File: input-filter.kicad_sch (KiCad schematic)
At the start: 28 parts

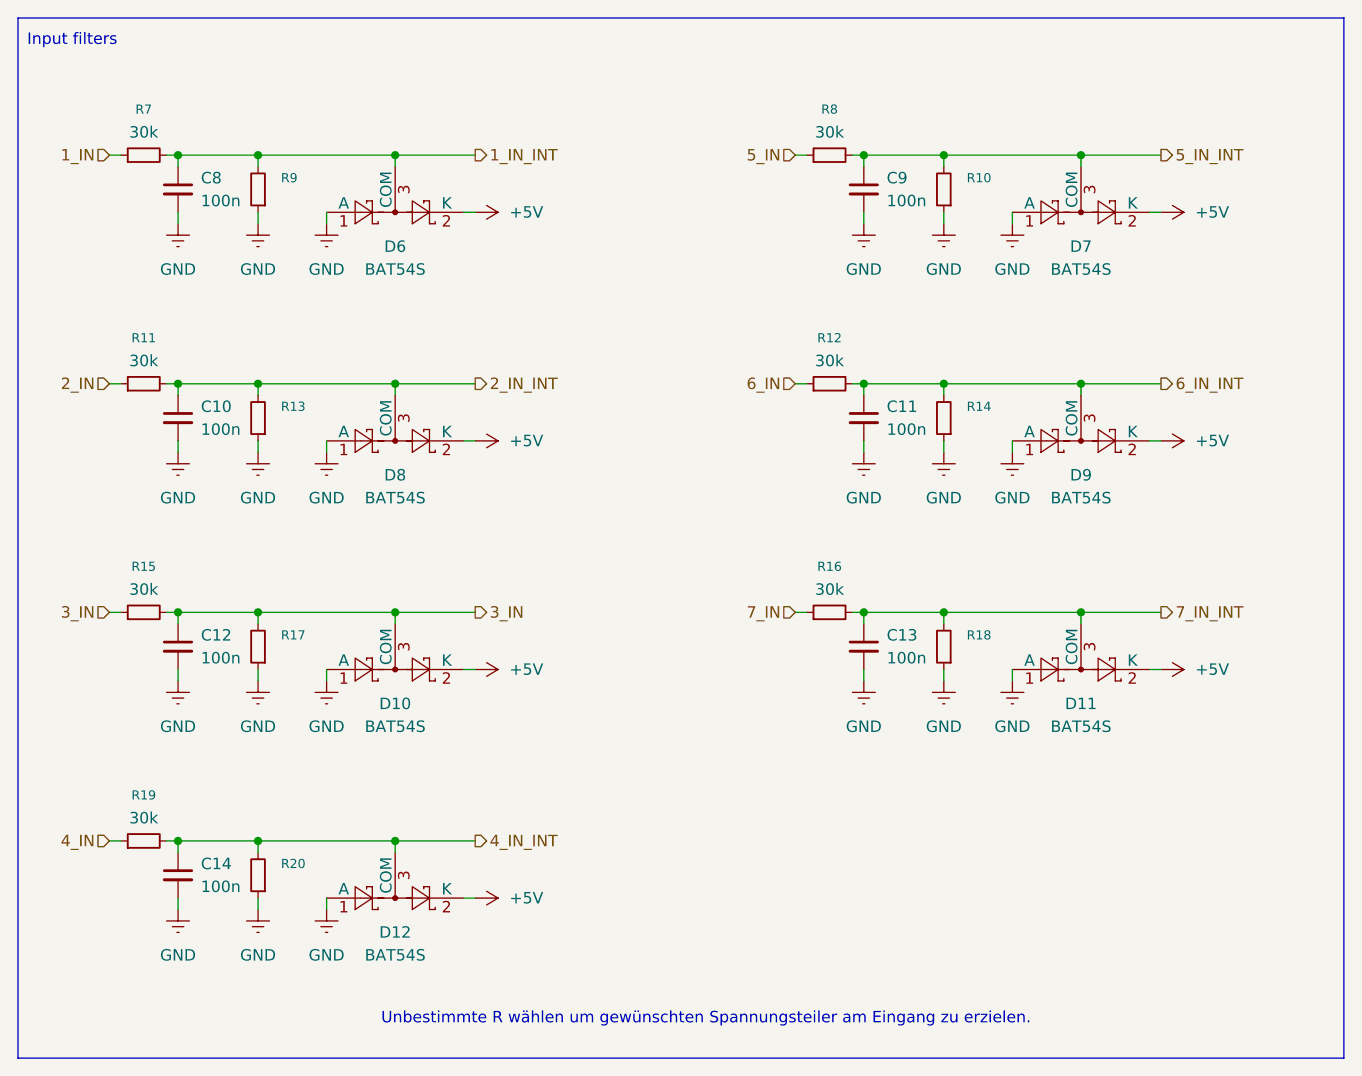
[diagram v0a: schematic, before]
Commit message: change voltage regulators
change can transciever
add more useful parts to can setup
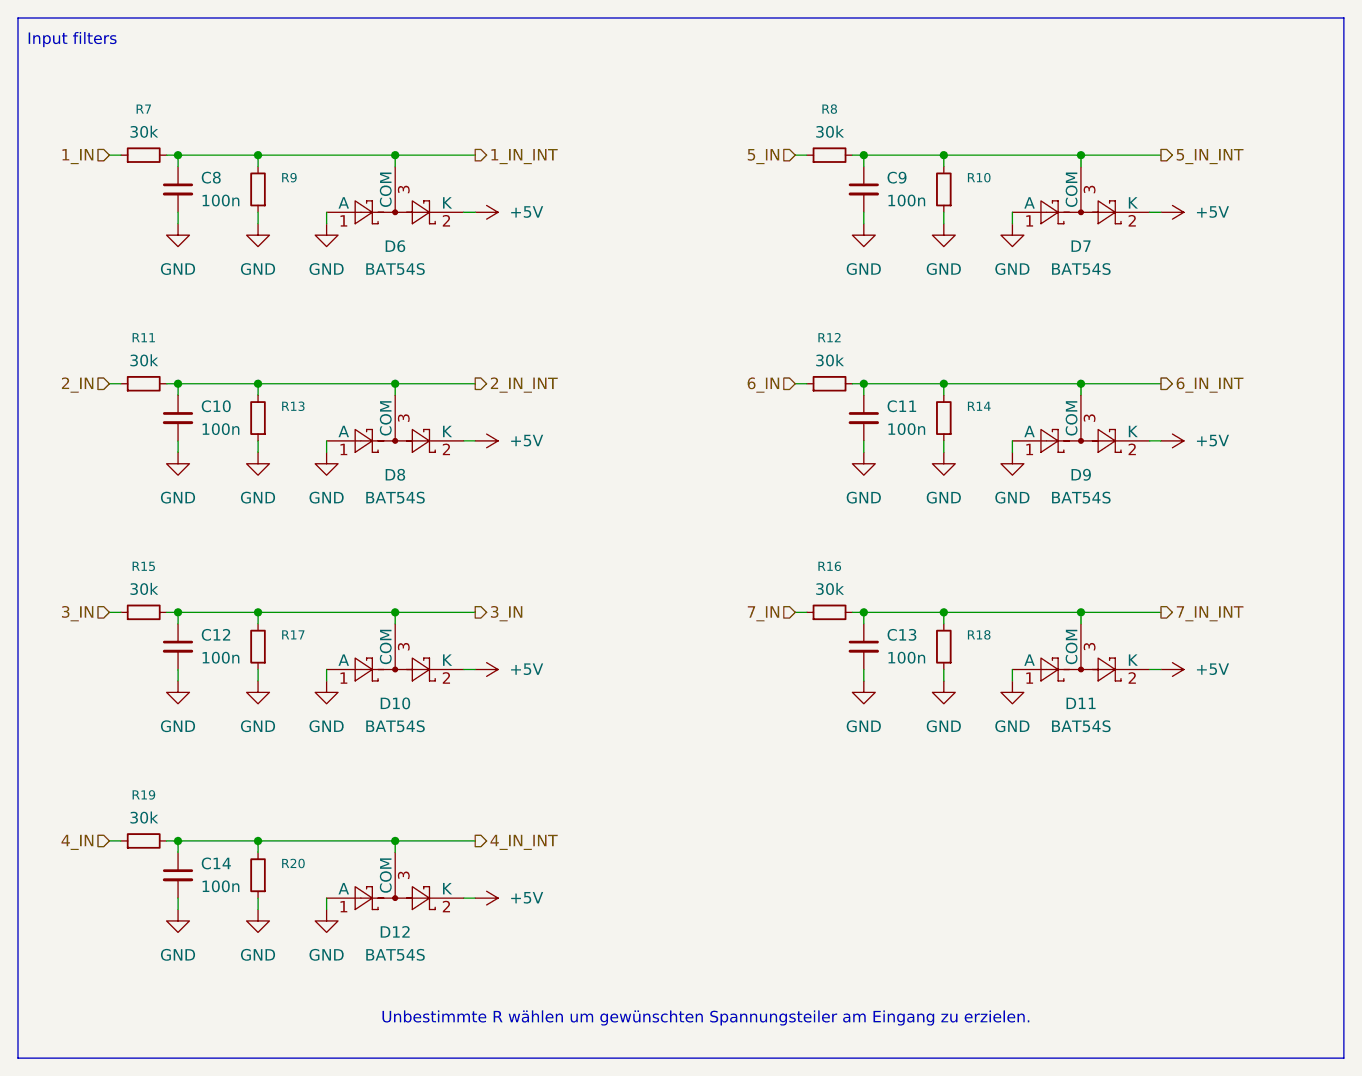
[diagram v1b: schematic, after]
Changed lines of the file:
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@@
 	)
 	(symbol
-		(lib_id "power:GNDREF")
+		(lib_id "power:GND")
 		(at 109.22 58.42 0)
 		(unit 1)
@@
 			)
 		)
-		(property "Description" "Power symbol creates a global label with name \"GNDREF\" , reference supply ground"
+		(property "Description" "Power symbol creates a global label with name \"GND\" , ground"
 			(at 109.22 58.42 0)
 			(effects
@@
 	)
 	(symbol
-		(lib_id "power:GNDREF")
+		(lib_id "power:GND")
 		(at 185.42 58.42 0)
 		(unit 1)
@@
 			)
 		)
-		(property "Description" "Power symbol creates a global label with name \"GNDREF\" , reference supply ground"
+		(property "Description" "Power symbol creates a global label with name \"GND\" , ground"
 			(at 185.42 58.42 0)
 			(effects
@@
 	)
 	(symbol
-		(lib_id "power:GNDREF")
+		(lib_id "power:GND")
 		(at 101.6 58.42 0)
 		(unit 1)
@@
 			)
 		)
-		(property "Description" "Power symbol creates a global label with name \"GNDREF\" , reference supply ground"
+		(property "Description" "Power symbol creates a global label with name \"GND\" , ground"
 			(at 101.6 58.42 0)
 			(effects
@@
 	)
 	(symbol
-		(lib_id "power:GNDREF")
+		(lib_id "power:GND")
 		(at 101.6 134.62 0)
 		(unit 1)
@@
 			)
 		)
-		(property "Description" "Power symbol creates a global label with name \"GNDREF\" , reference supply ground"
+		(property "Description" "Power symbol creates a global label with name \"GND\" , ground"
 			(at 101.6 134.62 0)
 			(effects
@@
 	)
 	(symbol
-		(lib_id "power:GNDREF")
+		(lib_id "power:GND")
 		(at 177.8 83.82 0)
 		(unit 1)
@@
 			)
 		)
-		(property "Description" "Power symbol creates a global label with name \"GNDREF\" , reference supply ground"
+		(property "Description" "Power symbol creates a global label with name \"GND\" , ground"
 			(at 177.8 83.82 0)
 			(effects
@@
 	)
 	(symbol
-		(lib_id "power:GNDREF")
+		(lib_id "power:GND")
 		(at 109.22 83.82 0)
 		(unit 1)
@@
 			)
 		)
-		(property "Description" "Power symbol creates a global label with name \"GNDREF\" , reference supply ground"
+		(property "Description" "Power symbol creates a global label with name \"GND\" , ground"
 			(at 109.22 83.82 0)
 			(effects
@@
 	)
 	(symbol
-		(lib_id "power:GNDREF")
+		(lib_id "power:GND")
 		(at 185.42 83.82 0)
 		(unit 1)
@@
 			)
 		)
-		(property "Description" "Power symbol creates a global label with name \"GNDREF\" , reference supply ground"
+		(property "Description" "Power symbol creates a global label with name \"GND\" , ground"
 			(at 185.42 83.82 0)
 			(effects
@@
 	)
 	(symbol
-		(lib_id "power:GNDREF")
+		(lib_id "power:GND")
 		(at 92.71 109.22 0)
 		(unit 1)
@@
 			)
 		)
-		(property "Description" "Power symbol creates a global label with name \"GNDREF\" , reference supply ground"
+		(property "Description" "Power symbol creates a global label with name \"GND\" , ground"
 			(at 92.71 109.22 0)
 			(effects
@@
 	)
 	(symbol
-		(lib_id "power:GNDREF")
+		(lib_id "power:GND")
 		(at 168.91 109.22 0)
 		(unit 1)
@@
 			)
 		)
-		(property "Description" "Power symbol creates a global label with name \"GNDREF\" , reference supply ground"
+		(property "Description" "Power symbol creates a global label with name \"GND\" , ground"
 			(at 168.91 109.22 0)
 			(effects
@@
 	)
 	(symbol
-		(lib_id "power:GNDREF")
+		(lib_id "power:GND")
 		(at 109.22 134.62 0)
 		(unit 1)
@@
 			)
 		)
-		(property "Description" "Power symbol creates a global label with name \"GNDREF\" , reference supply ground"
+		(property "Description" "Power symbol creates a global label with name \"GND\" , ground"
 			(at 109.22 134.62 0)
 			(effects
@@
 	)
 	(symbol
-		(lib_id "power:GNDREF")
+		(lib_id "power:GND")
 		(at 168.91 58.42 0)
 		(unit 1)
@@
 			)
 		)
-		(property "Description" "Power symbol creates a global label with name \"GNDREF\" , reference supply ground"
+		(property "Description" "Power symbol creates a global label with name \"GND\" , ground"
 			(at 168.91 58.42 0)
 			(effects
@@
 	)
 	(symbol
-		(lib_id "power:GNDREF")
+		(lib_id "power:GND")
 		(at 101.6 83.82 0)
 		(unit 1)
@@
 			)
 		)
-		(property "Description" "Power symbol creates a global label with name \"GNDREF\" , reference supply ground"
+		(property "Description" "Power symbol creates a global label with name \"GND\" , ground"
 			(at 101.6 83.82 0)
 			(effects
@@
 	)
 	(symbol
-		(lib_id "power:GNDREF")
+		(lib_id "power:GND")
 		(at 92.71 134.62 0)
 		(unit 1)
@@
 			)
 		)
-		(property "Description" "Power symbol creates a global label with name \"GNDREF\" , reference supply ground"
+		(property "Description" "Power symbol creates a global label with name \"GND\" , ground"
 			(at 92.71 134.62 0)
 			(effects
@@
 	)
 	(symbol
-		(lib_id "power:GNDREF")
+		(lib_id "power:GND")
 		(at 92.71 83.82 0)
 		(unit 1)
@@
 			)
 		)
-		(property "Description" "Power symbol creates a global label with name \"GNDREF\" , reference supply ground"
+		(property "Description" "Power symbol creates a global label with name \"GND\" , ground"
 			(at 92.71 83.82 0)
 			(effects
@@
 	)
 	(symbol
-		(lib_id "power:GNDREF")
+		(lib_id "power:GND")
 		(at 168.91 83.82 0)
 		(unit 1)
@@
 			)
 		)
-		(property "Description" "Power symbol creates a global label with name \"GNDREF\" , reference supply ground"
+		(property "Description" "Power symbol creates a global label with name \"GND\" , ground"
 			(at 168.91 83.82 0)
 			(effects
@@
 	)
 	(symbol
-		(lib_id "power:GNDREF")
+		(lib_id "power:GND")
 		(at 177.8 58.42 0)
 		(unit 1)
@@
 			)
 		)
-		(property "Description" "Power symbol creates a global label with name \"GNDREF\" , reference supply ground"
+		(property "Description" "Power symbol creates a global label with name \"GND\" , ground"
 			(at 177.8 58.42 0)
 			(effects
@@
 	)
 	(symbol
-		(lib_id "power:GNDREF")
+		(lib_id "power:GND")
 		(at 109.22 109.22 0)
 		(unit 1)
@@
 			)
 		)
-		(property "Description" "Power symbol creates a global label with name \"GNDREF\" , reference supply ground"
+		(property "Description" "Power symbol creates a global label with name \"GND\" , ground"
 			(at 109.22 109.22 0)
 			(effects
@@
 	)
 	(symbol
-		(lib_id "power:GNDREF")
+		(lib_id "power:GND")
 		(at 177.8 109.22 0)
 		(unit 1)
@@
 			)
 		)
-		(property "Description" "Power symbol creates a global label with name \"GNDREF\" , reference supply ground"
+		(property "Description" "Power symbol creates a global label with name \"GND\" , ground"
 			(at 177.8 109.22 0)
 			(effects
@@
 	)
 	(symbol
-		(lib_id "power:GNDREF")
+		(lib_id "power:GND")
 		(at 101.6 109.22 0)
 		(unit 1)
@@
 			)
 		)
-		(property "Description" "Power symbol creates a global label with name \"GNDREF\" , reference supply ground"
+		(property "Description" "Power symbol creates a global label with name \"GND\" , ground"
 			(at 101.6 109.22 0)
 			(effects
@@
 	)
 	(symbol
-		(lib_id "power:GNDREF")
+		(lib_id "power:GND")
 		(at 92.71 58.42 0)
 		(unit 1)
@@
 			)
 		)
-		(property "Description" "Power symbol creates a global label with name \"GNDREF\" , reference supply ground"
+		(property "Description" "Power symbol creates a global label with name \"GND\" , ground"
 			(at 92.71 58.42 0)
 			(effects
@@
 	)
 	(symbol
-		(lib_id "power:GNDREF")
+		(lib_id "power:GND")
 		(at 185.42 109.22 0)
 		(unit 1)
@@
 			)
 		)
-		(property "Description" "Power symbol creates a global label with name \"GNDREF\" , reference supply ground"
+		(property "Description" "Power symbol creates a global label with name \"GND\" , ground"
 			(at 185.42 109.22 0)
 			(effects

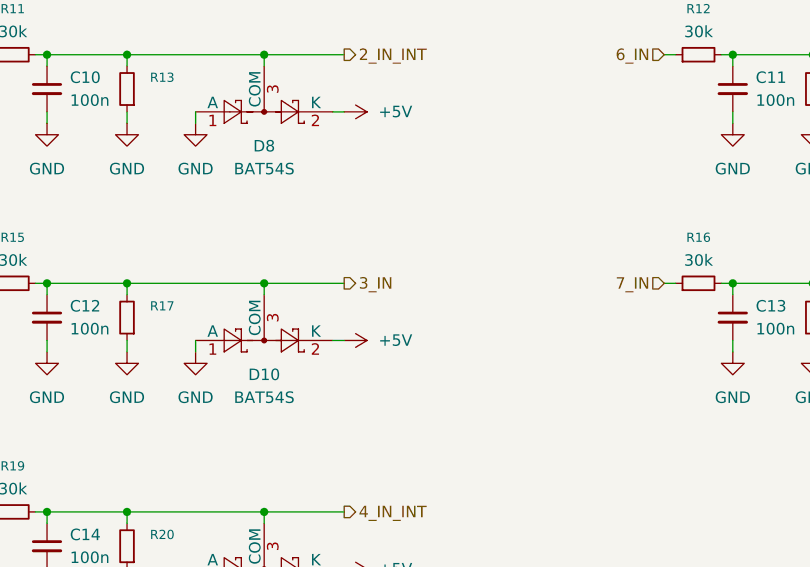
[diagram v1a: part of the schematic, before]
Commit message: added 6 axis imu LSM6DSV16BXTR
fixed link in in input filter
removed optional i2c
add not connected elements to ic
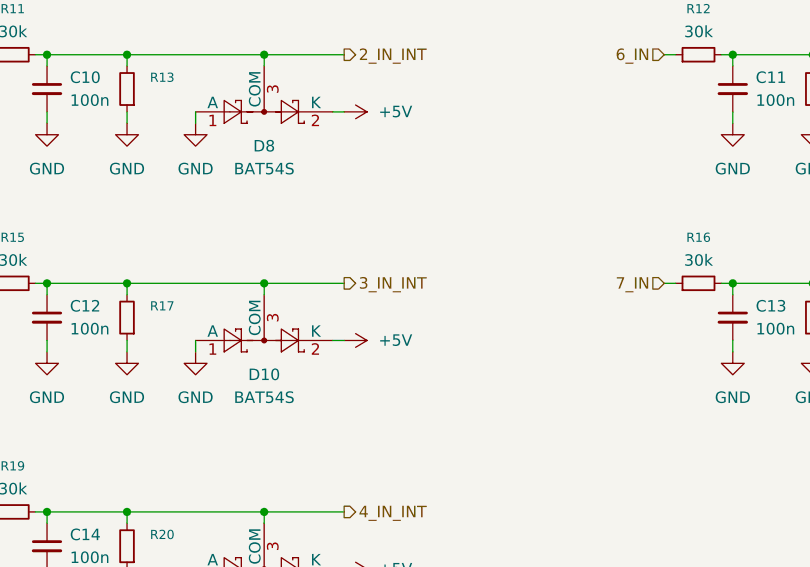
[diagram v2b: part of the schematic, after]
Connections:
- net 3_IN: no longer C12.1, D10.3 (COM), R15.2, R17.2
- new net 3_IN_INT: C12.1, D10.3 (COM), R15.2, R17.2
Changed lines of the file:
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@@
+		)
+	)
+	(hierarchical_label "3_IN_INT"
+		(shape output)
+		(at 125.73 101.6 0)
+		(effects
+			(font
+				(size 1.27 1.27)
+			)
+			(justify left)
 		)
 	)
@@
 		)
 	)
-	(hierarchical_label "3_IN"
-		(shape output)
-		(at 125.73 101.6 0)
-		(effects
-			(font
-				(size 1.27 1.27)
-			)
-			(justify left)
-		)
-	)

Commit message: group parts on pcb
replace footprints
update can setup
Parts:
- C10, C11, C12, C13, C14, C8, C9: footprint (none) -> Capacitor_SMD:C_0603_1608Metric
- R10, R11, R12, R13, R14, R15, R16, R17, R18, R19, R20, R7, R8, R9: footprint (none) -> Resistor_SMD:R_0603_1608Metric
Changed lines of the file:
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@@
 			)
 		)
-		(property "Footprint" ""
+		(property "Footprint" "Capacitor_SMD:C_0603_1608Metric"
 			(at 168.91 80.01 0)
 			(effects
@@
 			)
 		)
-		(property "Footprint" ""
+		(property "Footprint" "Resistor_SMD:R_0603_1608Metric"
 			(at 88.9 50.8 0)
 			(effects
@@
 			)
 		)
-		(property "Footprint" ""
+		(property "Footprint" "Resistor_SMD:R_0603_1608Metric"
 			(at 177.8 105.41 0)
 			(effects
@@
 			)
 		)
-		(property "Footprint" ""
+		(property "Footprint" "Capacitor_SMD:C_0603_1608Metric"
 			(at 92.71 130.81 0)
 			(effects
@@
 			)
 		)
-		(property "Footprint" ""
+		(property "Footprint" "Resistor_SMD:R_0603_1608Metric"
 			(at 165.1 101.6 0)
 			(effects
@@
 			)
 		)
-		(property "Footprint" ""
+		(property "Footprint" "Resistor_SMD:R_0603_1608Metric"
 			(at 101.6 130.81 0)
 			(effects
@@
 			)
 		)
-		(property "Footprint" ""
+		(property "Footprint" "Capacitor_SMD:C_0603_1608Metric"
 			(at 92.71 80.01 0)
 			(effects
@@
 			)
 		)
-		(property "Footprint" ""
+		(property "Footprint" "Resistor_SMD:R_0603_1608Metric"
 			(at 101.6 80.01 0)
 			(effects
@@
 			)
 		)
-		(property "Footprint" ""
+		(property "Footprint" "Resistor_SMD:R_0603_1608Metric"
 			(at 88.9 127 0)
 			(effects
@@
 			)
 		)
-		(property "Footprint" ""
+		(property "Footprint" "Resistor_SMD:R_0603_1608Metric"
 			(at 165.1 50.8 0)
 			(effects
@@
 			)
 		)
-		(property "Footprint" ""
+		(property "Footprint" "Capacitor_SMD:C_0603_1608Metric"
 			(at 92.71 105.41 0)
 			(effects
@@
 			)
 		)
-		(property "Footprint" ""
+		(property "Footprint" "Resistor_SMD:R_0603_1608Metric"
 			(at 88.9 101.6 0)
 			(effects
@@
 			)
 		)
-		(property "Footprint" ""
+		(property "Footprint" "Capacitor_SMD:C_0603_1608Metric"
 			(at 92.71 54.61 0)
 			(effects
@@
 			)
 		)
-		(property "Footprint" ""
+		(property "Footprint" "Resistor_SMD:R_0603_1608Metric"
 			(at 177.8 80.01 0)
 			(effects
@@
 			)
 		)
-		(property "Footprint" ""
+		(property "Footprint" "Capacitor_SMD:C_0603_1608Metric"
 			(at 168.91 105.41 0)
 			(effects
@@
 			)
 		)
-		(property "Footprint" ""
+		(property "Footprint" "Resistor_SMD:R_0603_1608Metric"
 			(at 101.6 105.41 0)
 			(effects
@@
 			)
 		)
-		(property "Footprint" ""
+		(property "Footprint" "Resistor_SMD:R_0603_1608Metric"
 			(at 101.6 54.61 0)
 			(effects
@@
 			)
 		)
-		(property "Footprint" ""
+		(property "Footprint" "Resistor_SMD:R_0603_1608Metric"
 			(at 165.1 76.2 0)
 			(effects
@@
 			)
 		)
-		(property "Footprint" ""
+		(property "Footprint" "Capacitor_SMD:C_0603_1608Metric"
 			(at 168.91 54.61 0)
 			(effects
@@
 			)
 		)
-		(property "Footprint" ""
+		(property "Footprint" "Resistor_SMD:R_0603_1608Metric"
 			(at 177.8 54.61 0)
 			(effects
@@
 			)
 		)
-		(property "Footprint" ""
+		(property "Footprint" "Resistor_SMD:R_0603_1608Metric"
 			(at 88.9 76.2 0)
 			(effects
